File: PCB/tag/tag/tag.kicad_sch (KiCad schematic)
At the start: 7 parts, among them J1 SM02B-SRSS-TB LFSN, J2 Conn_ARM_SWD_TagConnect_TC203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, J3 Conn_ARM_JTAG_SWD_10, U1 DWM3001C, U2 TPS79933DDCR

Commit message: pcb stuff
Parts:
- added C3: 100nF, symbol Device:C
- added C4: 10uF, symbol Device:C
- added J4: TSM-102-01-X-SV, TSM-102-01-X-SV:SAMTEC_TSM-102-01-X-SV, symbol sdp:TSM-102-01-X-SV
- added R1, R2: 1K5, symbol Device:R_US
- added R3, R4: 100K, symbol Device:R_US
- added R5: 150, symbol Device:R_US
- added R6: 820, symbol Device:R_US
- added S1: TL3315NF160Q, digikey-footprints:Switch_Tactile_SMD_4.5x4.5mm_TL3315NF160Q, symbol dk_Tactile-Switches:TL3315NF160Q
- added TP1, TP2, TP3, TP4, TP7: TestPoint, symbol Connector:TestPoint
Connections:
- net GND: now also C3.2, C4.2, R3.2, R4.2, S1.3, S1.4, TP1.1, TP7.1
- net RESET: now also S1.1, S1.2
- net Vreg: now also J4.01, TP3.1; no longer J2.1 (VCC), J3.1 (VTref), U1.12 (VDD)
- net SWD_DIO: now reaches J2.2 (SWDIO), J3.2 (SWDIO/TMS), U1.3 (SWD_DIO)
- net SWD_CLK: now reaches J2.4 (SWCLK), J3.4 (SWCLK/TCK), U1.2 (SWD_CLK)
- net at J1.1, U2.1 (IN), U2.3 (EN): now also TP2.1
- net at U1.44 (DW_GP3): now also R1.1
- net at U1.45 (DW_GP2): now also R2.1
- new net: C3.1, C4.1, J4.02, U1.12 (VDD)
- new net: R2.2, R4.1
- new net: R1.2, R3.1
- new net VDD: R5.1, R6.1
- no-connect marks 42 -> 40
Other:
- note added: "Programming Headers - Pin Header and Edge-Connect"
- note added: "Voltage Regulator"
- moved on the sheet: C1, C2, J1, J2, J3, U1, U2

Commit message: updated Tag PCB
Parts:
- added D1: LTST-C235KGKRKT, LED_SMD:LED_LiteOn_LTST-C235KGKRKT, symbol LED:LTST-C235KGKRKT
- added D2, D3: LED, symbol Device:LED
- added J5: TSM-102-01-X-SV, TSM-102-01-X-SV:SAMTEC_TSM-102-01-X-SV, symbol sdp:TSM-102-01-X-SV
- added Q1, Q2: IRLML2402TRPBF, digikey-footprints:SOT-23-3, symbol dk_Transistors-FETs-MOSFETs-Single:IRLML2402TRPBF
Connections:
- net VDD is gone; now on net Vreg: R5.1, R6.1
- net GND: now also J5.01
- net Vreg: now also D2.2 (A), D3.2 (A)
- net at R5.2: now also D1.2 (A2)
- net at R2.2, R4.1: now also Q2.1 (G)
- net at R1.2, R3.1: now also Q1.1 (G)
- net at U1.6 (P0.17): now also D3.1 (K)
- net at U1.7 (P0.14): now also D2.1 (K)
- net at R6.2: now also D1.3 (A1)
- new net: J5.02, Q1.2 (S), Q2.2 (S)
- new net: D1.1 (K2), Q1.3 (D)
- new net: D1.4 (K1), Q2.3 (D)
- no-connect marks 40 -> 38
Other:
- note added: "Programming Headers"
- note added: "Qorvo Combo Module and Test Peripheral"
- note removed: "Programming Headers - Pin Header and Edge-Connect"
- title: (none) -> BareTag_Tag
- moved on the sheet: C1, C2, C3, C4, J1, J2, J3, J4, R1, R2, R3, R4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

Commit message: updated Tag PCB
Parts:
- added R7, R8: 1k8, symbol Device:R_US
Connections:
- net at D3.1 (K): now also R8.1; no longer U1.6 (P0.17)
- net at U1.7 (P0.14): now also R7.2; no longer D2.1 (K)
- new net: R8.2, U1.6 (P0.17)
- new net: D2.1 (K), R7.1
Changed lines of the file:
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@@
 	(wire
 		(pts
+			(xy 120.65 49.53) (xy 120.65 59.69)
+		)
+		(stroke
+			(width 0)
+			(type default)
+		)
+	)
+	(wire
+		(pts
 			(xy 215.9 80.01) (xy 207.01 80.01)
 		)
@@
 	(wire
 		(pts
+			(xy 120.65 67.31) (xy 120.65 69.85)
+		)
+		(stroke
+			(width 0)
+			(type default)
+		)
+	)
+	(wire
+		(pts
 			(xy 229.87 64.77) (xy 229.87 69.85)
 		)
@@
 	(wire
 		(pts
+			(xy 120.65 69.85) (xy 161.29 69.85)
+		)
+		(stroke
+			(width 0)
+			(type default)
+		)
+	)
+	(wire
+		(pts
 			(xy 260.35 49.53) (xy 265.43 49.53)
 		)
@@
 	(wire
 		(pts
-			(xy 161.29 69.85) (xy 120.65 69.85)
+			(xy 129.54 49.53) (xy 129.54 59.69)
 		)
 		(stroke
@@
 	(wire
 		(pts
-			(xy 129.54 49.53) (xy 129.54 67.31)
-		)
-		(stroke
-			(width 0)
-			(type default)
-		)
-	)
-	(wire
-		(pts
 			(xy 265.43 132.08) (xy 265.43 135.89)
 		)
@@
 	(wire
 		(pts
-			(xy 120.65 49.53) (xy 120.65 69.85)
-		)
-		(stroke
-			(width 0)
-			(type default)
-		)
-	)
-	(wire
-		(pts
 			(xy 233.68 77.47) (xy 233.68 93.98)
 		)
@@
 	)
 	(symbol
+		(lib_id "Device:R_US")
+		(at 129.54 63.5 0)
+		(unit 1)
+		(exclude_from_sim no)
+		(in_bom yes)
+		(on_board yes)
+		(dnp no)
+		(fields_autoplaced yes)
+		(property "Reference" "R8"
+			(at 132.08 62.2299 0)
+			(effects
+				(font
+					(size 1.27 1.27)
+				)
+				(justify left)
+			)
+		)
+		(property "Value" "1k8"
+			(at 132.08 64.7699 0)
+			(effects
+				(font
+					(size 1.27 1.27)
+				)
+				(justify left)
+			)
+		)
+		(property "Footprint" ""
+			(at 130.556 63.754 90)
+			(effects
+				(font
+					(size 1.27 1.27)
+				)
+				(hide yes)
+			)
+		)
+		(property "Datasheet" "~"
+			(at 129.54 63.5 0)
+			(effects
+				(font
+					(size 1.27 1.27)
+				)
+				(hide yes)
+			)
+		)
+		(property "Description" "Resistor, US symbol"
+			(at 129.54 63.5 0)
+			(effects
+				(font
+					(size 1.27 1.27)
+				)
+				(hide yes)
+			)
+		)
+		(pin "2"
+		)
+		(pin "1"
+		)
+		(instances
+			(project ""
+				(path "/a33ba61a-a364-42a4-8098-b44cce0b54f2"
+					(reference "R8")
+					(unit 1)
+				)
+			)
+		)
+	)
+	(symbol
 		(lib_id "Connector:Conn_ARM_JTAG_SWD_10")
 		(at 36.83 77.47 0)
@@
 					(unit 1)
 				)
+			)
+		)
+	)
+	(symbol
+		(lib_id "Device:R_US")
+		(at 120.65 63.5 0)
+		(unit 1)
+		(exclude_from_sim no)
+		(in_bom yes)
+		(on_board yes)
+		(dnp no)
+		(property "Reference" "R7"
+			(at 115.57 62.23 0)
+			(effects
+				(font
+					(size 1.27 1.27)
+				)
+				(justify left)
+			)
+		)
+		(property "Value" "1k8"
+			(at 115.062 64.77 0)
+			(effects
+				(font
+					(size 1.27 1.27)
+				)
+				(justify left)
+			)
+		)
+		(property "Footprint" ""
+			(at 121.666 63.754 90)
+			(effects
+				(font
+					(size 1.27 1.27)
+				)
+				(hide yes)
+			)
+		)
+		(property "Datasheet" "~"
+			(at 120.65 63.5 0)
+			(effects
+				(font
+					(size 1.27 1.27)
+				)
+				(hide yes)
+			)
+		)
+		(property "Description" "Resistor, US symbol"
+			(at 120.65 63.5 0)
+			(effects
+				(font
+					(size 1.27 1.27)
+				)
+				(hide yes)
+			)
+		)
+		(pin "2"
+		)
+		(pin "1"
+		)
+		(instances
+			(project ""
+				(path "/a33ba61a-a364-42a4-8098-b44cce0b54f2"
+					(reference "R7")
+					(unit 1)
+				)

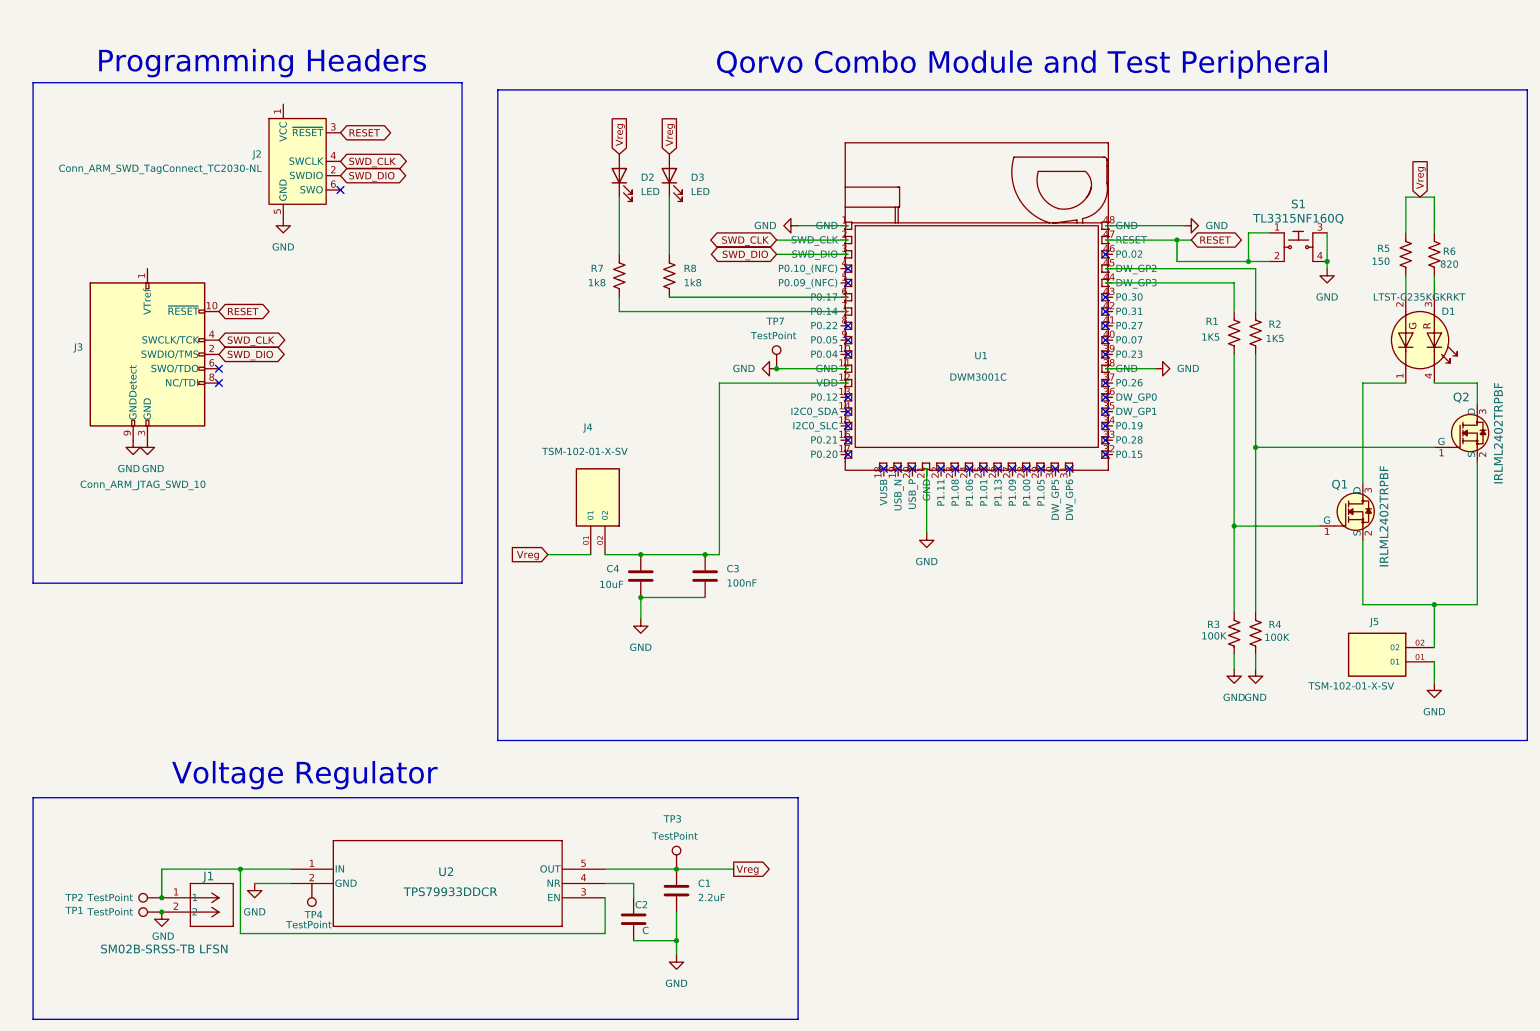
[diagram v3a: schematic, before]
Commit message: Tag and Anchor schematic updates
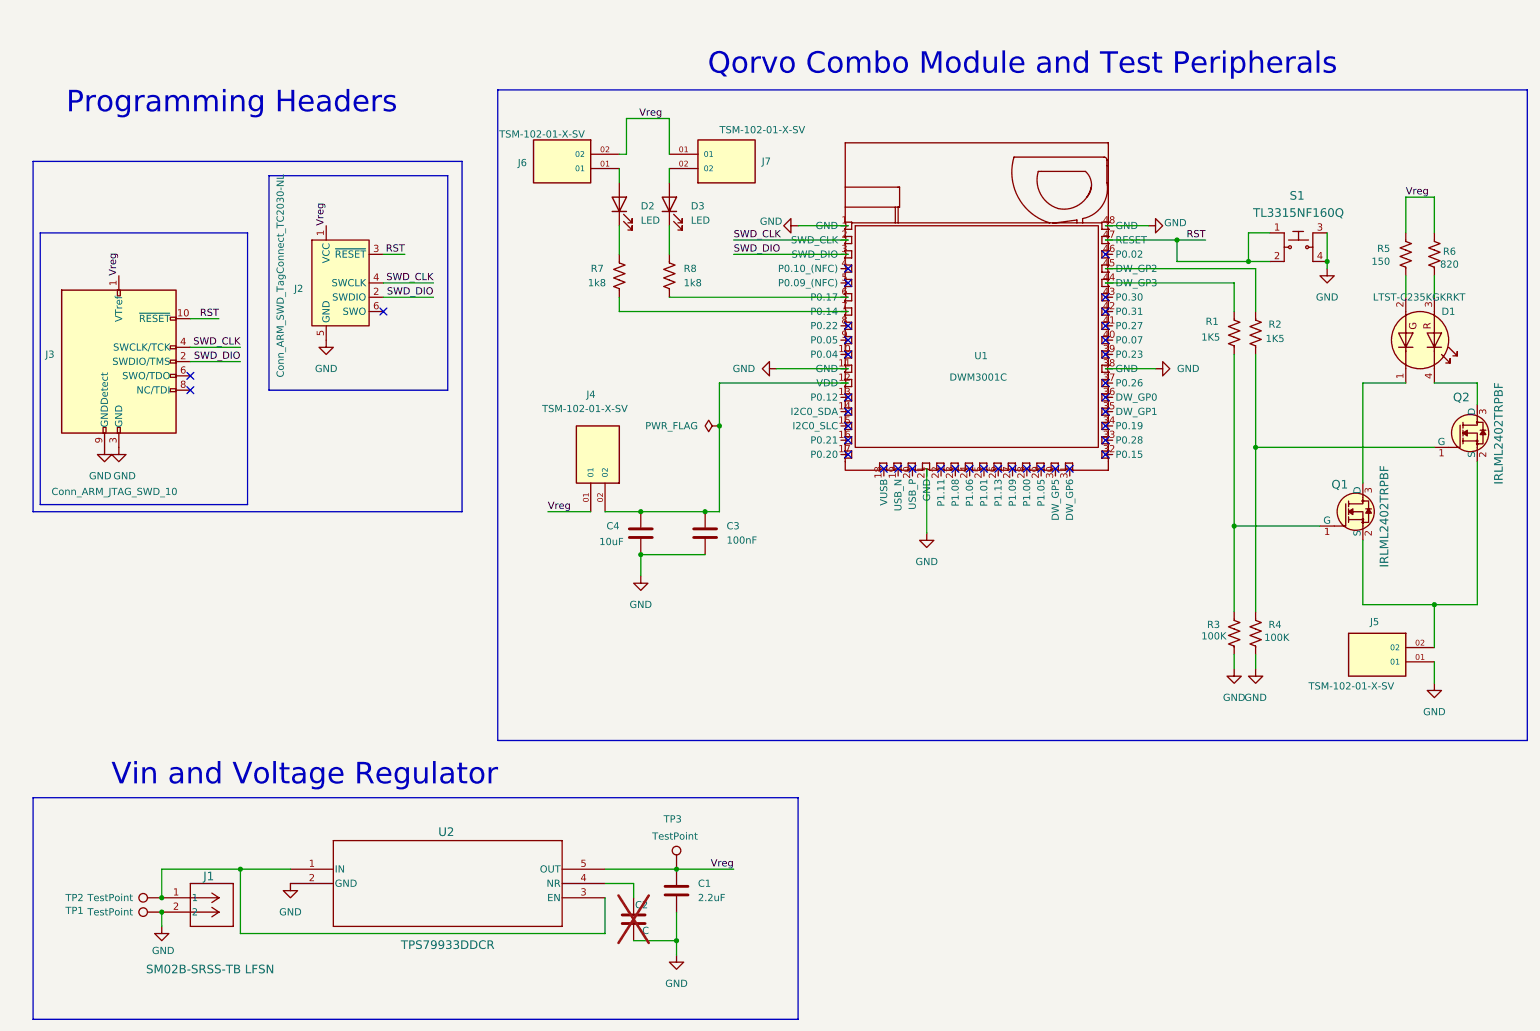
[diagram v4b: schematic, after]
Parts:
- removed TP4, TP7: TestPoint, symbol Connector:TestPoint
- added J6, J7: TSM-102-01-X-SV, TSM-102-01-X-SV:SAMTEC_TSM-102-01-X-SV, symbol sdp:TSM-102-01-X-SV
- C2: now not fitted
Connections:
- net Vreg: now also J2.1 (VCC), J3.1 (VTref), J6.02, J7.01; no longer D2.2 (A), D3.2 (A)
- net RESET renamed RST
- new net: D2.2 (A), J6.01
- new net: D3.2 (A), J7.02
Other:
- note added: "Qorvo Combo Module and Test Peripherals"
- note added: "Vin and Voltage Regulator"
- note removed: "Qorvo Combo Module and Test Peripheral"
- note removed: "Voltage Regulator"
- moved on the sheet: C3, C4, D2, D3, J2, J3, J4

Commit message: update
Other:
- moved on the sheet: U1

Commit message: maybe updates?
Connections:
- net Vreg: no longer C1.2, J2.1 (VCC), J3.1 (VTref), J4.01, J6.02, J7.01, TP3.1, U2.5 (OUT)
- net Vbatt +3.7V: now reaches J1.1, TP2.1, U2.1 (IN), U2.3 (EN)
- net LED GPIO Wires: now reaches R7.2, U1.7 (P0.14)
- new net Vreg +3.3V: C1.2, J2.1 (VCC), J3.1 (VTref), J4.01, J6.02, J7.01, TP3.1, U2.5 (OUT)
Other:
- company: (none) -> SDP Team 3
- moved on the sheet: J2, TP1, TP2

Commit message: PCB updates
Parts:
- D2, D3: value LED -> 150060RS75000
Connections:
- net Vreg is gone; now on net Vreg +3.3V: R5.1, R6.1

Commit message: this is the newest folder status
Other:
- note added: "Power Inputs"
- note removed: "Vin and Voltage Regulator"
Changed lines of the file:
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@@
 		)
 	)
-	(text "Vin and Voltage Regulator"
+	(text "Power Inputs"
 		(exclude_from_sim no)
 		(at 86.106 152.654 0)
